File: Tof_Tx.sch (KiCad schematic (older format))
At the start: 59 parts, among them M1 mounting_holes_laser, M2 mounting_holes_laser, U10 NC7WZ00K8X, U11 UMCC_50Ohm, U12 UMCC_50Ohm, U13 NC7WZ00K8X, U14 NCP81074BDR2G, U4 UMCC_50Ohm, U5 UMCC_50Ohm, U6 HMC589AST89E, U7 TLV3501, U8 UMCC_50Ohm, U9 NC7WZ00K8X

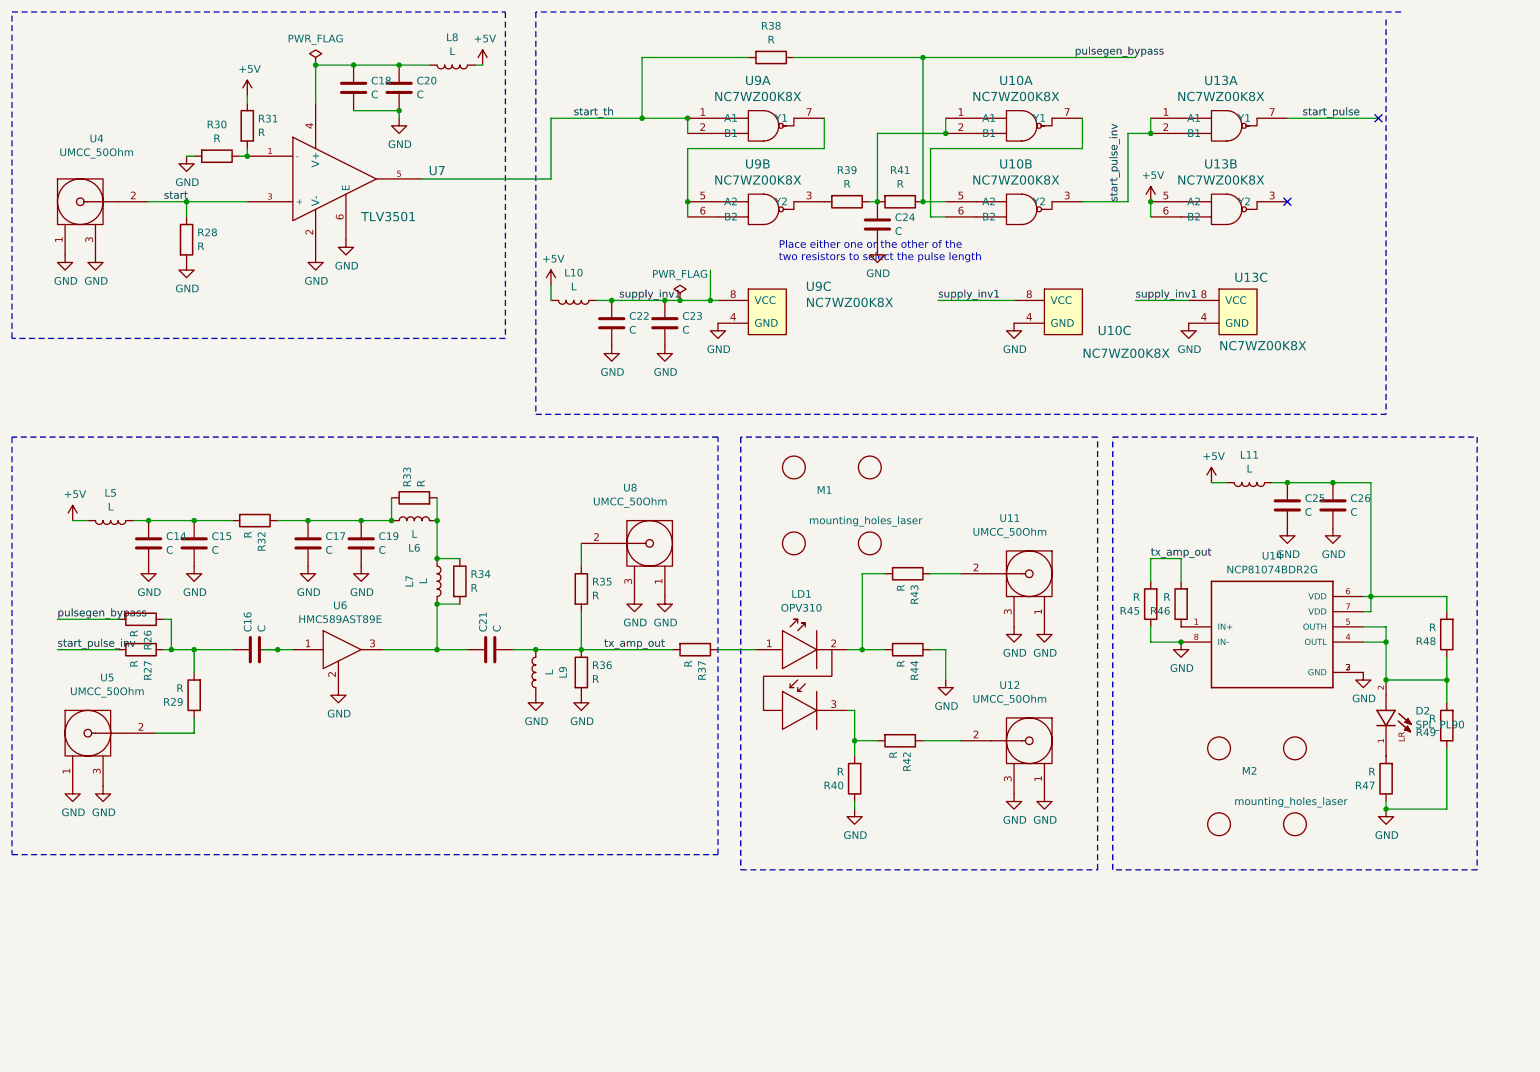
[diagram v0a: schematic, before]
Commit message: Added RLC values
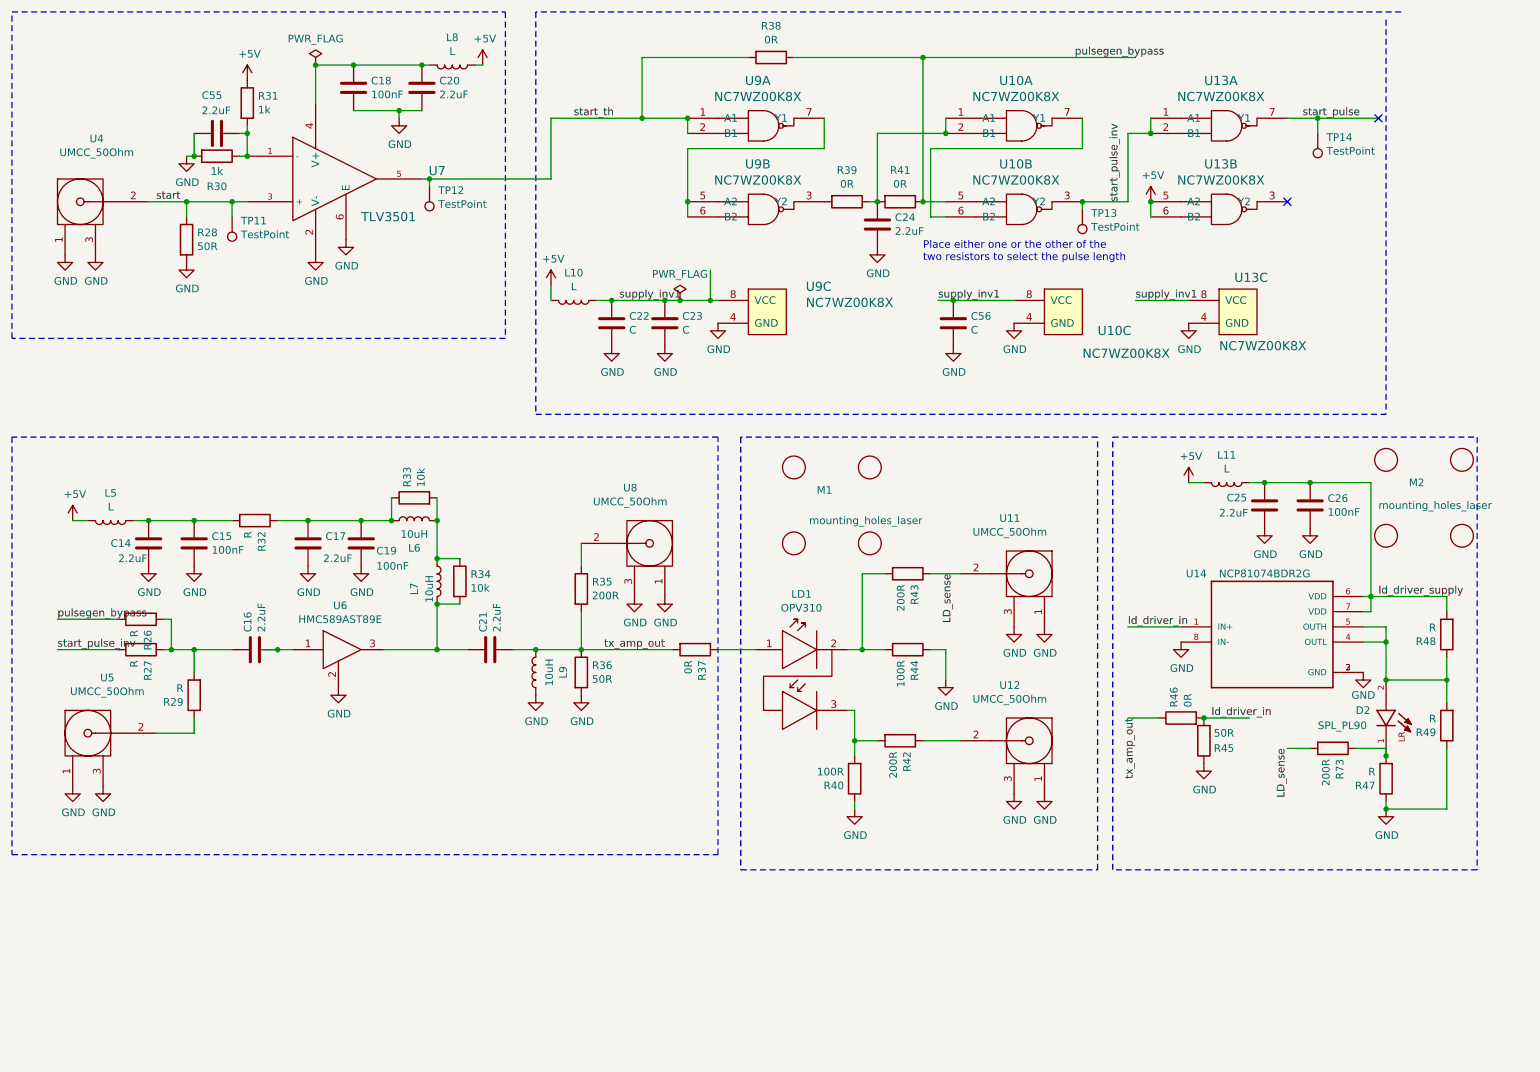
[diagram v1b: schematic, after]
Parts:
- added C55: 2.2uF, Capacitor_SMD:C_0603_1608Metric, symbol Device:C
- added C56: C, Capacitor_SMD:C_0603_1608Metric, symbol Device:C
- added R73: 200R, Resistor_SMD:R_0603_1608Metric, symbol Device:R
- added TP11, TP12, TP13, TP14: TestPoint, TestPoint:TestPoint_Pad_1.0x1.0mm, symbol Connector:TestPoint
- C14, C16, C17, C20, C21, C24, C25: value C -> 2.2uF
- C15, C18, C19, C26: value C -> 100nF
- L6, L7, L9: value L -> 10uH
- R28, R36, R45: value R -> 50R
- R30, R31: value R -> 1k
- R33, R34: value R -> 10k
- R35, R42, R43: value R -> 200R
- R37, R38, R39, R41, R46: value R -> 0R
- R40, R44: value R -> 100R
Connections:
- net labels added: LD_sense, ld_driver_in, ld_driver_supply
- wire segments 123 -> 135
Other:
- moved on the sheet: C20, C25, C26, L11, M2, R31, R45, R46

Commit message: Added more digikey numbers in BOM
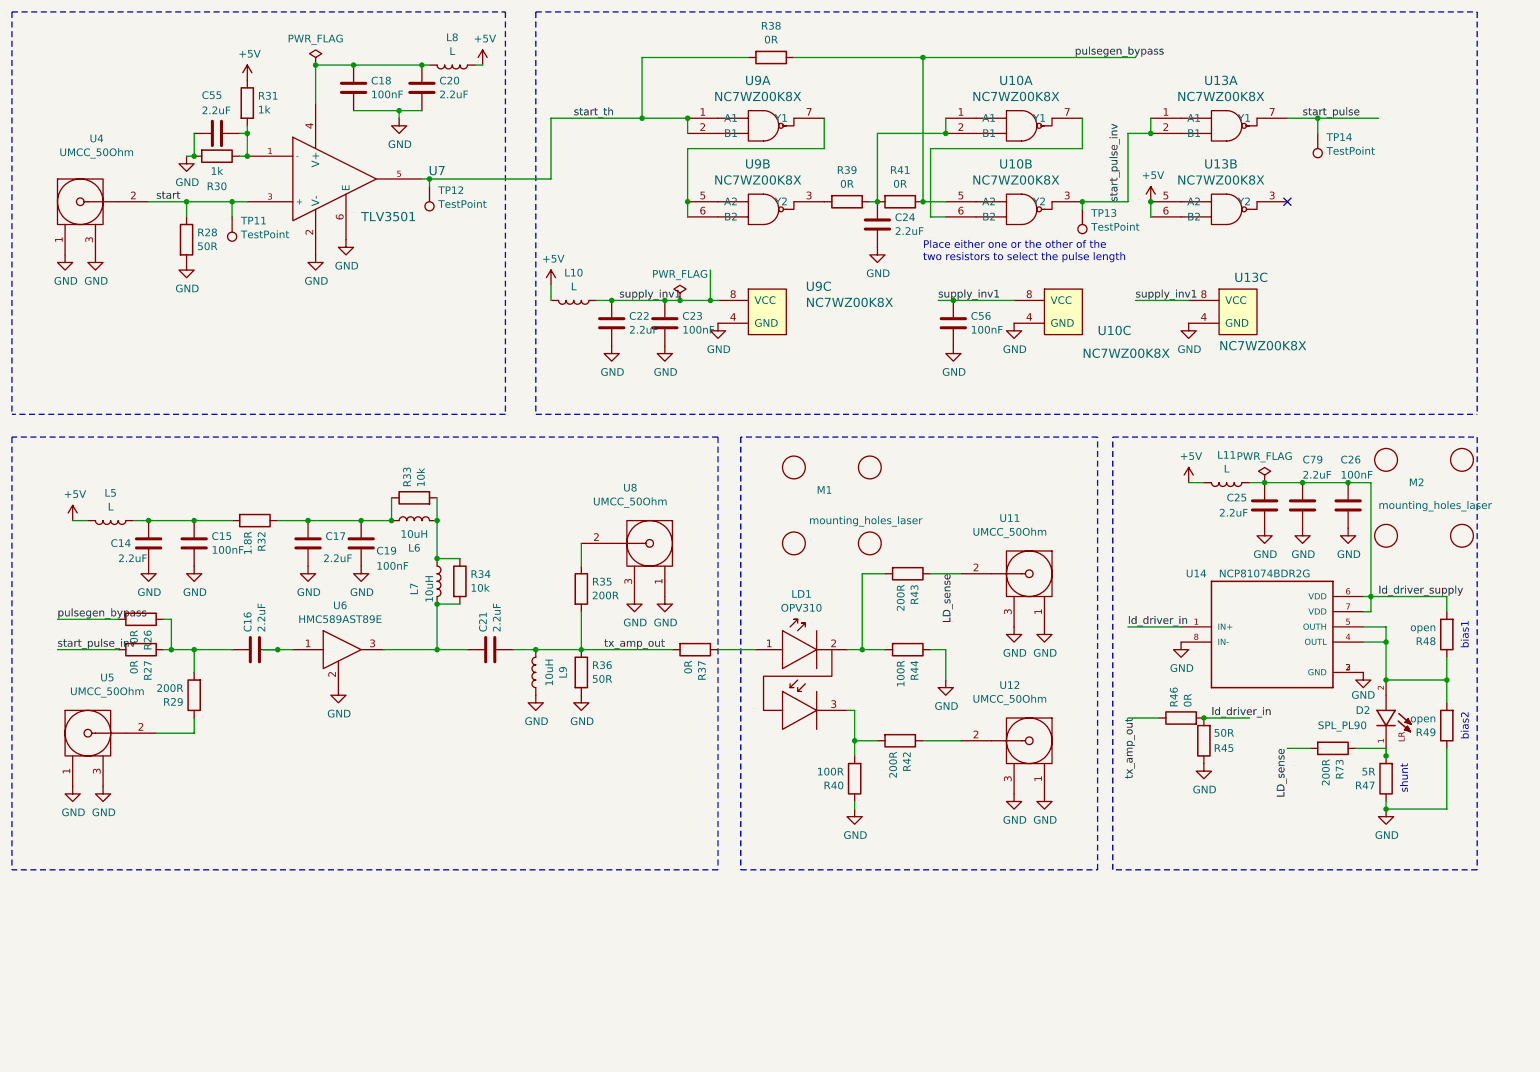
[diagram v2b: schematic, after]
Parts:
- added C79: 2.2uF, Capacitor_SMD:C_0603_1608Metric, symbol Device:C
- C22: value C -> 2.2uF
- C23, C56: value C -> 100nF
- D2: Digi-Key_PN (none) -> 475-3533-ND
- L10, L11, L5, L8: Digi-Key_PN (none) -> 490-5216-1-ND
- LD1: Digi-Key_PN (none) -> 365-1879-ND
- R26, R27: value R -> 0R
- R29: value R -> 200R
- R32: value R -> 1.8R
- R47: value R -> 5R
- R48, R49: value R -> open
- U10, U13, U9: Digi-Key_PN (none) -> NC7WZ00K8XCT-ND
- U11, U12, U4, U5, U8: Digi-Key_PN (none) -> A118077CT-ND
- U14: Digi-Key_PN (none) -> NCP81074BDR2GOSCT-ND
- U6: Digi-Key_PN (none) -> 1127-3329-1-ND
- U7: Digi-Key_PN (none) -> 296-43611-1-ND
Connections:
- wire segments 135 -> 136
- no-connect marks 2 -> 1
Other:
- note added: "bias1"
- note added: "bias2"
- note added: "shunt"
- moved on the sheet: C26

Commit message: bugfixes
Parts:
- added C82: 100nF, Capacitor_SMD:C_0603_1608Metric, symbol Device:C
- added C83: 2.2uF, Capacitor_SMD:C_0603_1608Metric, symbol Device:C
- added D6: LED, LEDs:LED_0805, symbol Device:LED
- added R84: 2.2k, Resistor_SMD:R_0603_1608Metric, symbol Device:R
- added R86: 200R, Resistor_SMD:R_0603_1608Metric, symbol Device:R
- added R87: 0R, Resistor_SMD:R_0603_1608Metric, symbol Device:R
- added U34: NC7WZ16, IODA_Lib:SOT65P210X110-6N, symbol ioda:NC7WZ16
- C14, C16, C17, C20, C21, C22, C25, C55, C79: Digi-Key_PN (none) -> 490-12740-1-ND
- C15, C18, C19, C23, C26, C56: Digi-Key_PN (none) -> 490-3285-1-ND
- C24: value 2.2uF -> c_tx_filt; Configuration (none) -> do not mount
- D2, LD1, R48, R49: Configuration (none) -> do not mount
- L10, L11, L5, L8: value L -> bead
- L6, L7, L9: Digi-Key_PN (none) -> 490-4025-1-ND
- R26, R38, R41, R46: Configuration (none) -> do not mount; Digi-Key_PN (none) -> RMCF0603ZT0R00CT-ND
- R27, R37, R39: Digi-Key_PN (none) -> RMCF0603ZT0R00CT-ND
- R28, R45: Digi-Key_PN (none) -> 541-56.0SCT-ND; Field4 (none) -> P49.9HCT-ND
- R29, R35, R42, R43, R73: Digi-Key_PN (none) -> RHM200ADCT-ND
- R30, R31: value 1k -> 2.2k; Digi-Key_PN (none) -> RMCF0603FT2K20CT-ND
- R32: Digi-Key_PN (none) -> 541-1.80CCCT-ND
- R33, R34: Digi-Key_PN (none) -> P10.0KHCT-ND
- R36: Configuration (none) -> do not mount; Digi-Key_PN (none) -> 541-56.0SCT-ND; Field4 (none) -> P49.9HCT-ND
- R40, R44: Digi-Key_PN (none) -> RMCF0603FT100R
- R47: value 5R -> 4.7R; Digi-Key_PN (none) -> RNCP0603FTD4R70CT-ND
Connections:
- net labels added: pg_bypass, pulse_inv, start_out, supply_th
- net labels removed: pulsegen_bypass, start_pulse_inv
- wire segments 136 -> 147
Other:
- moved on the sheet: C22, C23, C24, C55, C56, L10, L11, R31, R38, R39, R41, TP12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

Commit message: Version 1.0. As ordered at PCBWay on 13.11.2019
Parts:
- renumbered C14 to C28, C15 to C29, C55 to C30, C16 to C31, C17 to C32, C18 to C33, C19 to C34, C20 to C35, C21 to C36, C22 to C37, C23 to C38, C24 to C39, C56 to C40, C82 to C41, C83 to C42, C25 to C43, C79 to C44, C26 to C45, D6 to D3, D2 to D4, L9 to L10, L10 to L11, L11 to L12, L5 to L6, L6 to L7, L7 to L8, L8 to L9, R26 to R35, R27 to R36, R86 to R37, R28 to R38, R29 to R39, R84 to R40, R30 to R41, R31 to R42, R32 to R43, R33 to R44, R34 to R45, R35 to R46, R36 to R47, R37 to R48, R87 to R49, R38 to R50, R40 to R51, R42 to R52, R43 to R53, R44 to R54, R39 to R55, R41 to R56, R46 to R57, R45 to R58, R73 to R59, R47 to R60, R48 to R61, R49 to R62, TP11 to TP6, TP12 to TP7, TP13 to TP8, TP14 to TP9, U34 to U10, U8 to U11, U9 to U12, U10 to U13, U11 to U14, U12 to U15, U13 to U16, U14 to U17, U4 to U6, U5 to U7, U6 to U8, U7 to U9

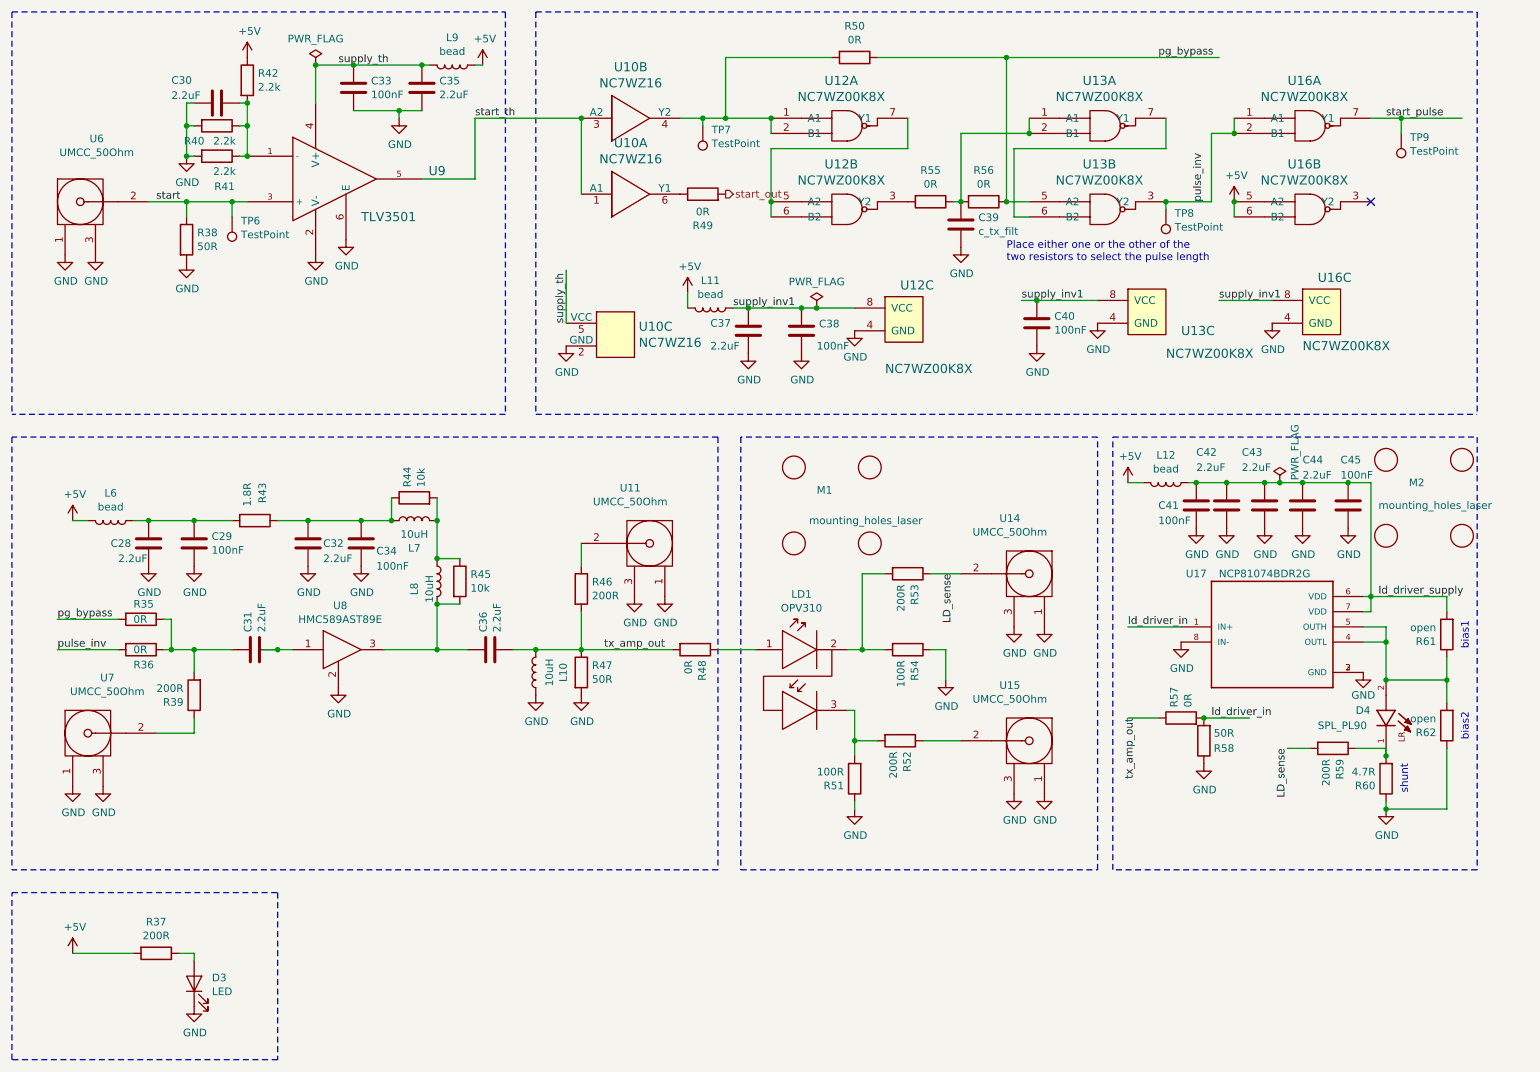
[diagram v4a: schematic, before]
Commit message: This is the actual pcb ordered by PCBWay 13.11.2019 The last commit had an error in the schematic files
Revert "Version 1.0. As ordered at PCBWay on 13.11.2019"

This reverts commit d90296e8e464a35f67a5ff7ebe731cf47d5f6555.
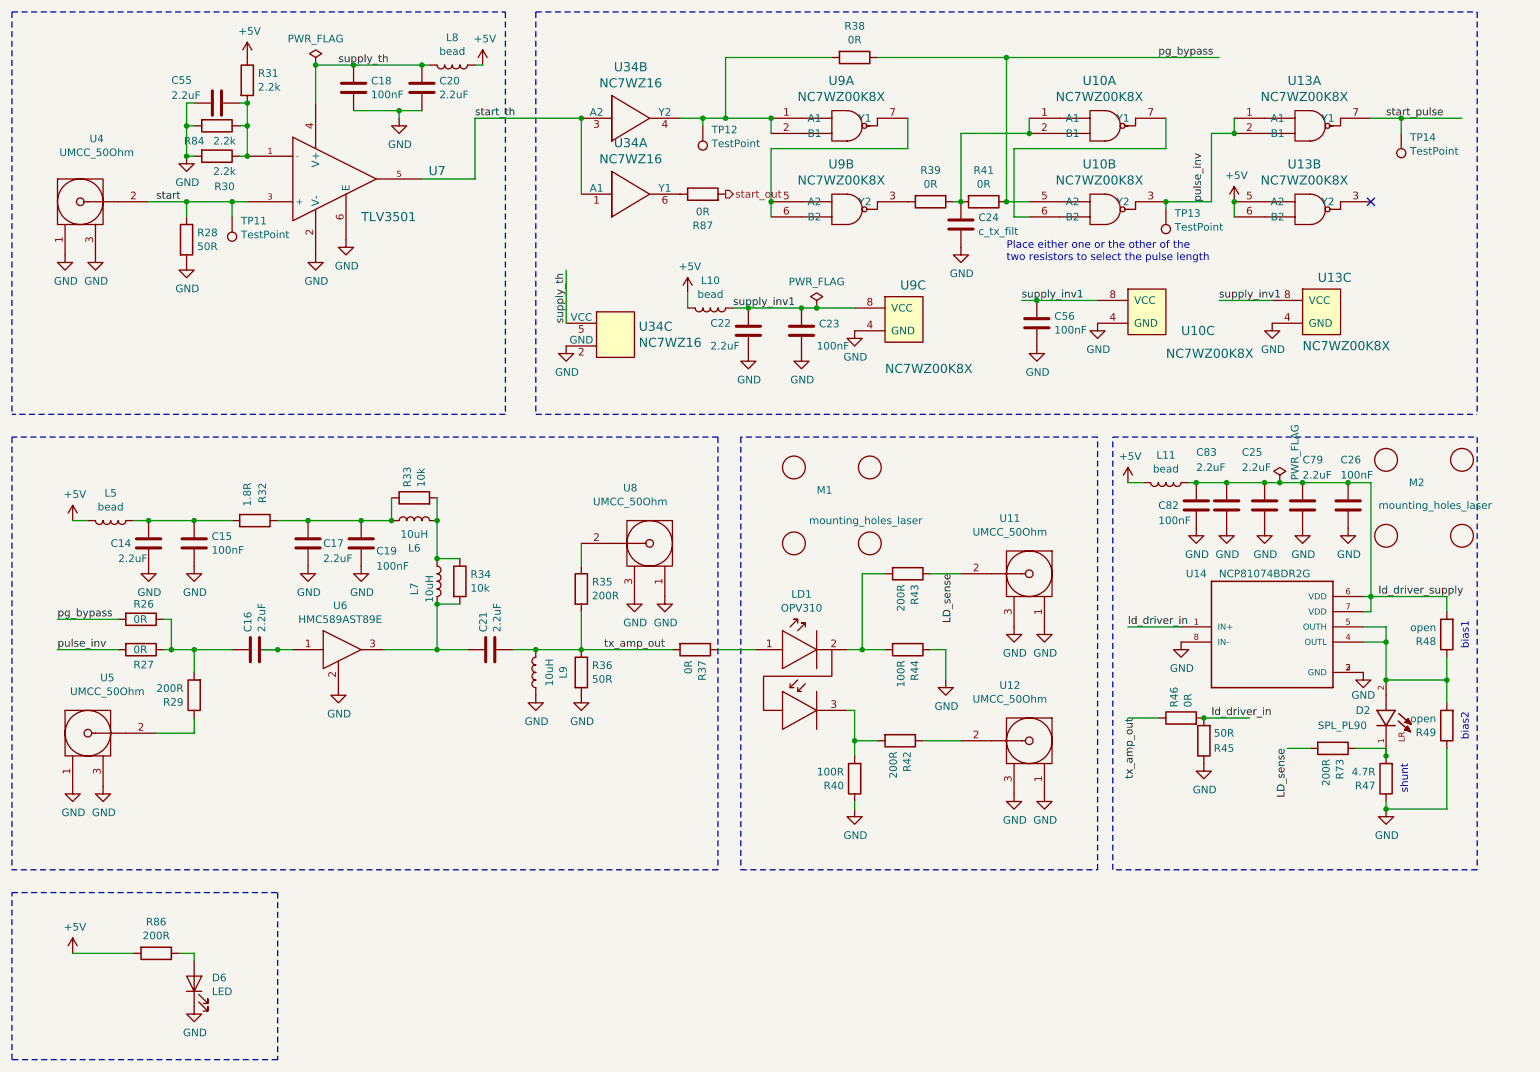
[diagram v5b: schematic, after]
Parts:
- renumbered C28 to C14, C29 to C15, C31 to C16, C32 to C17, C33 to C18, C34 to C19, C35 to C20, C36 to C21, C37 to C22, C38 to C23, C39 to C24, C43 to C25, C45 to C26, C30 to C55, C40 to C56, C44 to C79, C41 to C82, C42 to C83, D4 to D2, D3 to D6, L11 to L10, L12 to L11, L6 to L5, L7 to L6, L8 to L7, L9 to L8, L10 to L9, R35 to R26, R36 to R27, R38 to R28, R39 to R29, R41 to R30, R42 to R31, R43 to R32, R44 to R33, R45 to R34, R46 to R35, R47 to R36, R48 to R37, R50 to R38, R55 to R39, R51 to R40, R56 to R41, R52 to R42, R53 to R43, R54 to R44, R58 to R45, R57 to R46, R60 to R47, R61 to R48, R62 to R49, R59 to R73, R40 to R84, R37 to R86, R49 to R87, TP6 to TP11, TP7 to TP12, TP8 to TP13, TP9 to TP14, U13 to U10, U14 to U11, U15 to U12, U16 to U13, U17 to U14, U10 to U34, U6 to U4, U7 to U5, U8 to U6, U9 to U7, U11 to U8, U12 to U9

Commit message: changed 100k resistor and tlv3501 digikey numbers
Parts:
- U34: Digi-Key_PN NC7WZ16P6XCT-ND -> NC7WZ00K8XCT-ND
- U7: Digi-Key_PN 296-43611-1-ND -> 296-35977-1-ND
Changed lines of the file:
@@
 F 2 "IODA_Lib:SOT-23-6" H 3600 1800 50  0001 C CNN
 F 3 "https://www.ti.com/lit/ds/symlink/tlv3501.pdf" H 3600 1800 50  0001 C CNN
-F 4 "296-43611-1-ND" H 3600 1800 50  0001 C CNN "Digi-Key_PN"
+F 4 "296-35977-1-ND" H 3600 1800 50  0001 C CNN "Digi-Key_PN"
 	1    3600 1800
 	1    0    0    -1
@@
 F 2 "IODA_Lib:SOT65P210X110-6N" H 4875 2475 60  0001 C CNN
 F 3 "" H 5150 2000 60  0001 C CNN
-F 4 "NC7WZ16P6XCT-ND" H 4875 2375 50  0001 C CNN "Digi-Key_PN"
+F 4 "NC7WZ00K8XCT-ND" H 4875 2375 50  0001 C CNN "Digi-Key_PN"
 	1    5150 1900
 	1    0    0    -1
@@
 F 2 "IODA_Lib:SOT65P210X110-6N" H 4875 1975 60  0001 C CNN
 F 3 "" H 5150 1500 60  0001 C CNN
-F 4 "NC7WZ16P6XCT-ND" H 4875 1875 50  0001 C CNN "Digi-Key_PN"
+F 4 "NC7WZ00K8XCT-ND" H 4875 1875 50  0001 C CNN "Digi-Key_PN"
 	2    5150 1400
 	1    0    0    -1
@@
 F 2 "IODA_Lib:SOT65P210X110-6N" H 4975 3325 60  0001 C CNN
 F 3 "" H 5250 2850 60  0001 C CNN
-F 4 "NC7WZ16P6XCT-ND" H 4975 3225 50  0001 C CNN "Digi-Key_PN"
+F 4 "NC7WZ00K8XCT-ND" H 4975 3225 50  0001 C CNN "Digi-Key_PN"
 	3    5250 2750
 	1    0    0    -1
